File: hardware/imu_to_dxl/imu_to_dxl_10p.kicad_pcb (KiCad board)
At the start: 2 copper layers, 141.9 x 72.9 mm, 867 parts, among them CN1 B3B-EH-A (LF)(SN), CN2 B3B-PH-K-S(LF)(SN), J1 1.8mm螺丝孔, J2 1.8mm螺丝孔, J3 1.8mm螺丝孔, J4 1.8mm螺丝孔, Q1 MMBT3906, U1 ETA2845S2G_C22362741, U2 GD32F303CCT6, U3 LSM6DSV16XTR, U4 SN74LVC1G126DBVR, U5 SN74LVC1G125DBV, U6 ME6211C18M5G-N, X1 XL2EL89CSI-111YLC-12M

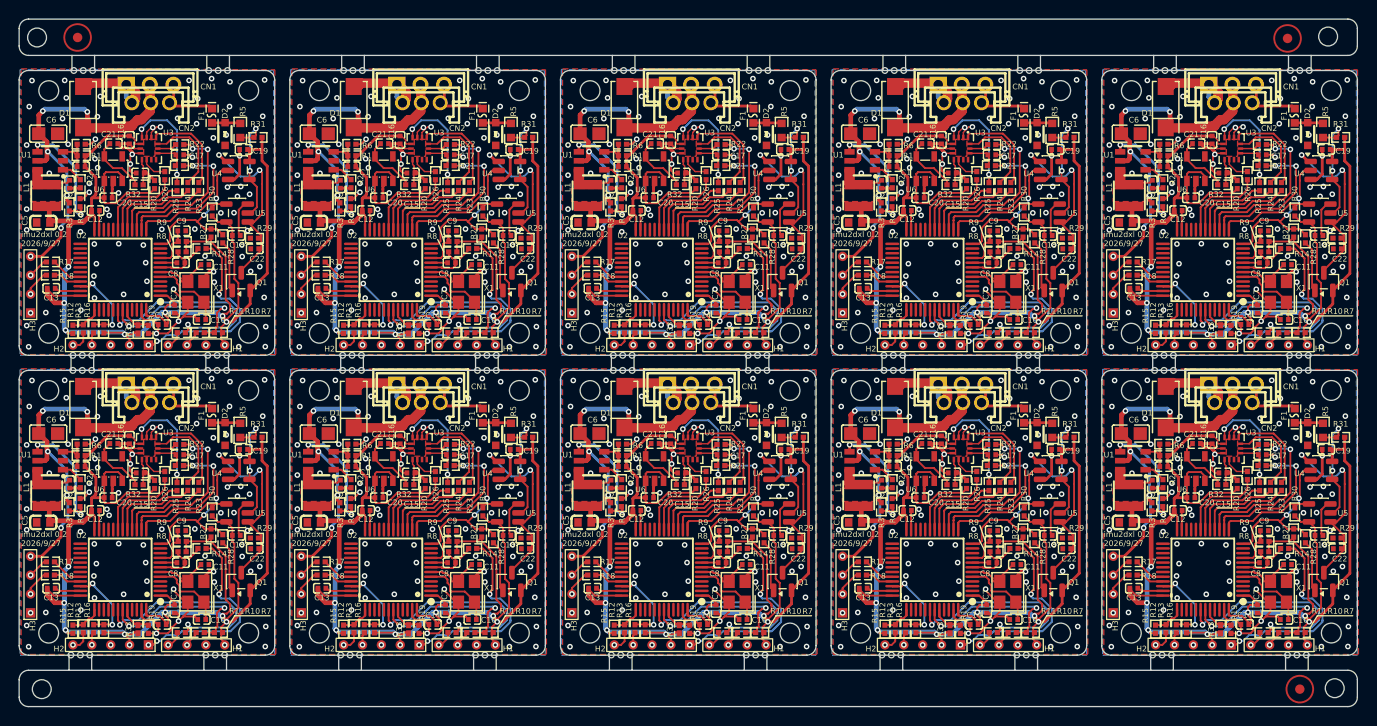
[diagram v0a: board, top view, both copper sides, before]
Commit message: 更新imu_to_dxl:1、优化MCU晶震电路；2、增加调试知识灯
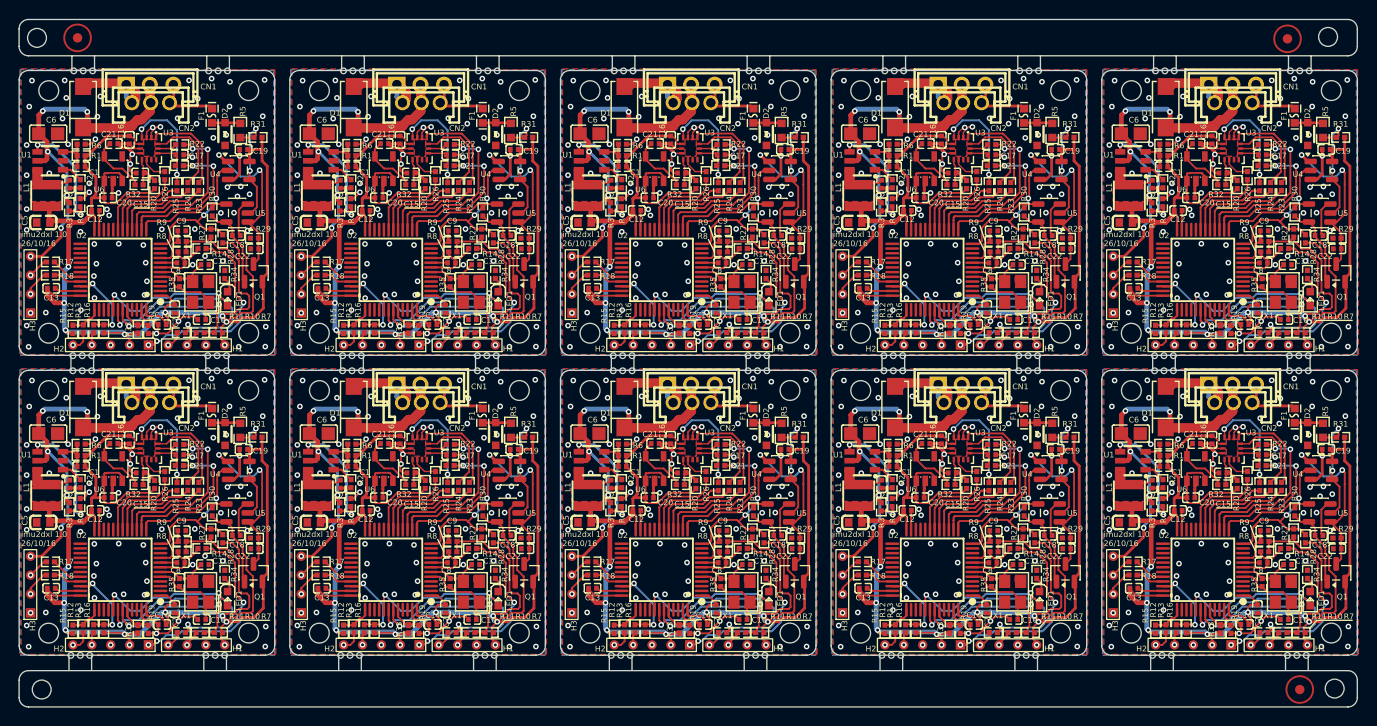
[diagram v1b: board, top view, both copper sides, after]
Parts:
- removed the Q1 at (133.6, 157.6)
- removed the Q1 at (162.2, 157.6)
- removed the Q1 at (76.2, 125.8)
- removed the Q1 at (190.9, 125.8)
- removed the Q1 at (76.2, 157.6)
- removed the Q1 at (162.2, 125.8)
- removed the Q1 at (104.8, 157.6)
- removed the Q1 at (133.6, 125.8)
- removed the Q1 at (104.8, 125.8)
- removed the REF** at (130.0, 103.4)
- removed the REF** at (189.3, 133.6)
- removed the REF** at (131.9, 135.2)
- removed the REF** at (72.6, 135.2)
- removed the REF** at (87.9, 135.2)
- removed the REF** at (60.1, 165.4)
- removed the REF** at (145.1, 165.4)
- removed the REF** at (55.0, 169.0)
- removed the REF** at (160.7, 103.4)
- removed the REF** at (187.4, 103.4)
- removed the REF** at (74.6, 133.6)
- removed the REF** at (116.7, 103.4)
- removed the REF** at (117.6, 135.2)
- removed the REF** at (116.4, 165.4)
- removed the REF** at (131.0, 103.4)
- removed the REF** at (72.7, 103.4)
- removed the REF** at (173.8, 165.4)
- removed the REF** at (145.3, 133.6)
- removed the REF** at (102.3, 103.4)
- removed the REF** at (160.6, 135.2)
- removed the REF** at (58.8, 99.9)
- removed the REF** at (87.7, 165.4)
- removed the REF** at (144.4, 103.4)
- removed the REF** at (103.2, 133.6)
- removed the REF** at (159.4, 165.4)
- removed the REF** at (131.9, 133.6)
- removed the REF** at (86.9, 133.6)
- removed the REF** at (60.3, 135.2)
- removed the REF** at (116.6, 135.2)
- removed the REF** at (160.4, 165.4)
- removed the REF** at (159.6, 133.6)
- removed the REF** at (131.7, 165.4)
- removed the REF** at (187.1, 100.0)
- removed the REF** at (88.0, 103.4)
- removed the REF** at (146.3, 135.2)
- removed the REF** at (173.1, 103.4)
- removed the REF** at (189.4, 103.4)
- removed the REF** at (188.4, 169.0)
- removed the REF** at (60.3, 133.6)
- removed the REF** at (58.3, 133.6)
- removed the REF** at (146.4, 103.4)
- removed the REF** at (102.2, 133.6)
- removed the REF** at (130.7, 165.4)
- removed the REF** at (129.9, 133.6)
- removed the REF** at (102.0, 165.4)
- removed the REF** at (174.8, 165.4)
- removed the REF** at (88.7, 165.4)
- removed the REF** at (117.7, 103.4)
- removed the REF** at (158.4, 165.4)
- removed the REF** at (115.6, 133.6)
- removed the REF** at (60.4, 103.4)
- removed the REF** at (101.3, 103.4)
- removed the REF** at (102.2, 135.2)
- removed the REF** at (144.3, 135.2)
- removed the REF** at (59.4, 103.4)
- removed the REF** at (132.0, 103.4)
- removed the REF** at (59.3, 133.6)
- removed the REF** at (159.6, 135.2)
- removed the REF** at (173.0, 133.6)
- removed the REF** at (130.9, 135.2)
- removed the REF** at (103.2, 135.2)
- removed the REF** at (158.6, 133.6)
- removed the REF** at (58.4, 103.4)
- removed the REF** at (189.1, 165.4)
- removed the REF** at (130.9, 133.6)
- removed the REF** at (188.3, 135.2)
- removed the REF** at (174.0, 135.2)
- removed the REF** at (103.3, 103.4)
- removed the REF** at (172.8, 165.4)
- removed the REF** at (144.1, 165.4)
- removed the REF** at (86.7, 165.4)
- removed the REF** at (87.9, 133.6)
- removed the REF** at (72.4, 165.4)
- removed the REF** at (175.1, 103.4)
- removed the REF** at (74.4, 165.4)
- removed the REF** at (187.3, 133.6)
- removed the REF** at (58.3, 135.2)
- removed the REF** at (188.1, 165.4)
- removed the REF** at (59.1, 165.4)
- removed the REF** at (188.4, 103.4)
- removed the REF** at (115.6, 135.2)
- removed the REF** at (73.7, 103.4)
- removed the REF** at (145.3, 135.2)
- removed the REF** at (146.1, 165.4)
- removed the REF** at (58.1, 165.4)
- removed the REF** at (116.6, 133.6)
- removed the REF** at (129.7, 165.4)
- removed the REF** at (187.1, 165.4)
- removed the REF** at (89.0, 103.4)
- removed the REF** at (101.2, 133.6)
- removed the REF** at (175.0, 135.2)
- removed the REF** at (145.4, 103.4)
- removed the REF** at (101.2, 135.2)
- removed the REF** at (173.0, 135.2)
- removed the REF** at (101.0, 165.4)
- removed the REF** at (72.6, 133.6)
- removed the REF** at (88.9, 133.6)
- removed the REF** at (160.6, 133.6)
- removed the REF** at (129.9, 135.2)
- removed the REF** at (187.3, 135.2)
- removed the REF** at (188.3, 133.6)
- removed the REF** at (144.3, 133.6)
- removed the REF** at (74.7, 103.4)
- removed the REF** at (158.7, 103.4)
- removed the REF** at (73.6, 133.6)
- removed the REF** at (115.4, 165.4)
- removed the REF** at (174.0, 133.6)
- removed the REF** at (189.3, 135.2)
- removed the REF** at (87.0, 103.4)
- removed the REF** at (146.3, 133.6)
- removed the REF** at (191.4, 99.8)
- removed the REF** at (174.1, 103.4)
- removed the REF** at (54.5, 99.9)
- removed the REF** at (175.0, 133.6)
- removed the REF** at (159.7, 103.4)
- removed the REF** at (192.1, 168.9)
- removed the REF** at (88.9, 135.2)
- removed the REF** at (74.6, 135.2)
- removed the REF** at (59.3, 135.2)
- removed the REF** at (73.6, 135.2)
- removed the REF** at (117.6, 133.6)
- removed the REF** at (158.6, 135.2)
- removed the REF** at (117.4, 165.4)
- removed the REF** at (115.7, 103.4)
- removed the REF** at (73.4, 165.4)
- removed the REF** at (86.9, 135.2)
- removed the REF** at (103.0, 165.4)
- removed the X1 at (157.4, 126.9)
- removed the X1 at (71.3, 126.9)
- removed the X1 at (100.0, 158.7)
- removed the X1 at (128.7, 158.7)
- removed the X1 at (186.1, 126.9)
- removed the X1 at (100.0, 126.9)
- removed the X1 at (128.7, 126.9)
- removed the X1 at (71.3, 158.7)
- removed the X1 at (157.4, 158.7)
- added LED1: GL0603UG01, microduck:LED0603-RD, F.Cu at (160.8, 159.4)
- added LED1: GL0603UG01, microduck:LED0603-RD, F.Cu at (160.8, 127.6)
- added LED1: GL0603UG01, microduck:LED0603-RD, F.Cu at (189.5, 159.4)
- added LED1: GL0603UG01, microduck:LED0603-RD, F.Cu at (103.4, 127.6)
- added LED1: GL0603UG01, microduck:LED0603-RD, F.Cu at (74.7, 127.6)
- added LED1: GL0603UG01, microduck:LED0603-RD, F.Cu at (74.7, 159.4)
- added LED1: GL0603UG01, microduck:LED0603-RD, F.Cu at (189.5, 127.6)
- added LED1: GL0603UG01, microduck:LED0603-RD, F.Cu at (103.4, 159.4)
- added LED1: GL0603UG01, microduck:LED0603-RD, F.Cu at (132.1, 127.6)
- added LED1: GL0603UG01, microduck:LED0603-RD, F.Cu at (132.1, 159.4)
- added Q1: MMBT3906, Package_TO_SOT_SMD:SOT-23, F.Cu at (77.5, 124.9)
- added Q1: MMBT3906, Package_TO_SOT_SMD:SOT-23, F.Cu at (77.5, 156.7)
- added Q1: MMBT3906, Package_TO_SOT_SMD:SOT-23, F.Cu at (106.2, 156.7)
- added Q1: MMBT3906, Package_TO_SOT_SMD:SOT-23, F.Cu at (106.2, 124.9)
- added Q1: MMBT3906, Package_TO_SOT_SMD:SOT-23, F.Cu at (134.8, 156.7)
- added Q1: MMBT3906, Package_TO_SOT_SMD:SOT-23, F.Cu at (192.2, 124.9)
- added Q1: MMBT3906, Package_TO_SOT_SMD:SOT-23, F.Cu at (134.8, 124.9)
- added Q1: MMBT3906, Package_TO_SOT_SMD:SOT-23, F.Cu at (163.6, 156.7)
- added Q1: MMBT3906, Package_TO_SOT_SMD:SOT-23, F.Cu at (163.6, 124.9)
- added R34: 100K, microduck:R0402, F.Cu at (131.8, 125.0)
- added R34: 100K, microduck:R0402, F.Cu at (74.4, 156.8)
- added R34: 100K, microduck:R0402, F.Cu at (160.5, 156.8)
- added R34: 100K, microduck:R0402, F.Cu at (189.2, 125.0)
- added R34: 100K, microduck:R0402, F.Cu at (160.5, 125.0)
- added R34: 100K, microduck:R0402, F.Cu at (103.1, 156.8)
- added R34: 100K, microduck:R0402, F.Cu at (189.2, 156.8)
- added R34: 100K, microduck:R0402, F.Cu at (103.1, 125.0)
- added R34: 100K, microduck:R0402, F.Cu at (131.8, 156.8)
- added R34: 100K, microduck:R0402, F.Cu at (74.4, 125.0)
- added R35: 1M, microduck:R0402, F.Cu at (155.7, 157.7)
- added R35: 1M, microduck:R0402, F.Cu at (155.7, 125.9)
- added R35: 1M, microduck:R0402, F.Cu at (127.0, 157.7)
- added R35: 1M, microduck:R0402, F.Cu at (69.6, 125.9)
- added R35: 1M, microduck:R0402, F.Cu at (98.3, 125.9)
- added R35: 1M, microduck:R0402, F.Cu at (69.6, 157.7)
- added R35: 1M, microduck:R0402, F.Cu at (127.0, 125.9)
- added R35: 1M, microduck:R0402, F.Cu at (98.3, 157.7)
- added R35: 1M, microduck:R0402, F.Cu at (184.4, 157.7)
- added R35: 1M, microduck:R0402, F.Cu at (184.4, 125.9)
- added REF**: mailslot, microduck:mailslot, F.Cu at (58.3, 133.6)
- added REF**: mailslot, microduck:mailslot, F.Cu at (160.4, 165.4)
- added REF**: mailslot, microduck:mailslot, F.Cu at (188.4, 103.4)
- added REF**: mailslot, microduck:mailslot, F.Cu at (103.0, 165.4)
- added REF**: mailslot, microduck:mailslot, F.Cu at (160.6, 133.6)
- added REF**: mailslot, microduck:mailslot, F.Cu at (115.6, 135.2)
- added REF**: mailslot, microduck:mailslot, F.Cu at (160.6, 135.2)
- added REF**: mailslot, microduck:mailslot, F.Cu at (174.1, 103.4)
- added REF**: mailslot, microduck:mailslot, F.Cu at (103.2, 135.2)
- added REF**: Mark, microduck:Mark, F.Cu at (187.1, 100.0)
- added REF**: mailslot, microduck:mailslot, F.Cu at (73.4, 165.4)
- added REF**: mailslot, microduck:mailslot, F.Cu at (103.3, 103.4)
- added REF**: mailslot, microduck:mailslot, F.Cu at (74.6, 133.6)
- added REF**: mailslot, microduck:mailslot, F.Cu at (174.0, 135.2)
- added REF**: mailslot, microduck:mailslot, F.Cu at (117.6, 133.6)
- added REF**: mailslot, microduck:mailslot, F.Cu at (145.3, 133.6)
- added REF**: mailslot, microduck:mailslot, F.Cu at (189.1, 165.4)
- added REF**: mailslot, microduck:mailslot, F.Cu at (144.4, 103.4)
- added REF**: mailslot, microduck:mailslot, F.Cu at (72.6, 135.2)
- added REF**: mailslot, microduck:mailslot, F.Cu at (89.0, 103.4)
- added REF**: Mark, microduck:Mark, F.Cu at (188.4, 169.0)
- added REF**: mailslot, microduck:mailslot, F.Cu at (101.3, 103.4)
- added REF**: mailslot, microduck:mailslot, F.Cu at (131.9, 135.2)
- added REF**: mailslot, microduck:mailslot, F.Cu at (88.7, 165.4)
- added REF**: mailslot, microduck:mailslot, F.Cu at (131.7, 165.4)
- added REF**: mailslot, microduck:mailslot, F.Cu at (173.8, 165.4)
- added REF**: INS_HOLE, microduck:INS_HOLE, F.Cu at (191.4, 99.8)
- added REF**: mailslot, microduck:mailslot, F.Cu at (187.3, 133.6)
- added REF**: mailslot, microduck:mailslot, F.Cu at (159.7, 103.4)
- added REF**: mailslot, microduck:mailslot, F.Cu at (189.4, 103.4)
- added REF**: mailslot, microduck:mailslot, F.Cu at (116.6, 133.6)
- added REF**: INS_HOLE, microduck:INS_HOLE, F.Cu at (55.0, 169.0)
- added REF**: mailslot, microduck:mailslot, F.Cu at (60.3, 135.2)
- added REF**: mailslot, microduck:mailslot, F.Cu at (59.1, 165.4)
- added REF**: mailslot, microduck:mailslot, F.Cu at (115.6, 133.6)
- added REF**: mailslot, microduck:mailslot, F.Cu at (102.0, 165.4)
- added REF**: mailslot, microduck:mailslot, F.Cu at (144.3, 135.2)
- added REF**: INS_HOLE, microduck:INS_HOLE, F.Cu at (192.1, 168.9)
- added REF**: mailslot, microduck:mailslot, F.Cu at (101.0, 165.4)
- added REF**: mailslot, microduck:mailslot, F.Cu at (145.1, 165.4)
- added REF**: mailslot, microduck:mailslot, F.Cu at (103.2, 133.6)
- added REF**: mailslot, microduck:mailslot, F.Cu at (144.3, 133.6)
- added REF**: mailslot, microduck:mailslot, F.Cu at (88.0, 103.4)
- added REF**: mailslot, microduck:mailslot, F.Cu at (72.6, 133.6)
- added REF**: mailslot, microduck:mailslot, F.Cu at (188.3, 133.6)
- added REF**: mailslot, microduck:mailslot, F.Cu at (187.4, 103.4)
- added REF**: mailslot, microduck:mailslot, F.Cu at (159.4, 165.4)
- added REF**: mailslot, microduck:mailslot, F.Cu at (101.2, 135.2)
- added REF**: mailslot, microduck:mailslot, F.Cu at (132.0, 103.4)
- added REF**: mailslot, microduck:mailslot, F.Cu at (117.4, 165.4)
- added REF**: mailslot, microduck:mailslot, F.Cu at (60.1, 165.4)
- added REF**: mailslot, microduck:mailslot, F.Cu at (58.4, 103.4)
- added REF**: mailslot, microduck:mailslot, F.Cu at (72.7, 103.4)
- added REF**: INS_HOLE, microduck:INS_HOLE, F.Cu at (54.5, 99.9)
- added REF**: mailslot, microduck:mailslot, F.Cu at (175.0, 133.6)
- added REF**: mailslot, microduck:mailslot, F.Cu at (86.9, 135.2)
- added REF**: mailslot, microduck:mailslot, F.Cu at (160.7, 103.4)
- added REF**: mailslot, microduck:mailslot, F.Cu at (159.6, 135.2)
- added REF**: mailslot, microduck:mailslot, F.Cu at (115.7, 103.4)
- added REF**: mailslot, microduck:mailslot, F.Cu at (60.4, 103.4)
- added REF**: mailslot, microduck:mailslot, F.Cu at (174.0, 133.6)
- added REF**: mailslot, microduck:mailslot, F.Cu at (74.7, 103.4)
- added REF**: mailslot, microduck:mailslot, F.Cu at (117.6, 135.2)
- added REF**: mailslot, microduck:mailslot, F.Cu at (146.4, 103.4)
- added REF**: mailslot, microduck:mailslot, F.Cu at (59.3, 135.2)
- added REF**: mailslot, microduck:mailslot, F.Cu at (59.4, 103.4)
- added REF**: mailslot, microduck:mailslot, F.Cu at (116.7, 103.4)
- added REF**: mailslot, microduck:mailslot, F.Cu at (87.9, 135.2)
- added REF**: mailslot, microduck:mailslot, F.Cu at (130.7, 165.4)
- added REF**: mailslot, microduck:mailslot, F.Cu at (73.6, 135.2)
- added REF**: mailslot, microduck:mailslot, F.Cu at (145.4, 103.4)
- added REF**: mailslot, microduck:mailslot, F.Cu at (74.6, 135.2)
- added REF**: mailslot, microduck:mailslot, F.Cu at (188.1, 165.4)
- added REF**: mailslot, microduck:mailslot, F.Cu at (87.7, 165.4)
- added REF**: mailslot, microduck:mailslot, F.Cu at (87.0, 103.4)
- added REF**: mailslot, microduck:mailslot, F.Cu at (60.3, 133.6)
- added REF**: mailslot, microduck:mailslot, F.Cu at (102.2, 133.6)
- added REF**: mailslot, microduck:mailslot, F.Cu at (172.8, 165.4)
- added REF**: mailslot, microduck:mailslot, F.Cu at (158.6, 135.2)
- added REF**: Mark, microduck:Mark, F.Cu at (58.8, 99.9)
- added REF**: mailslot, microduck:mailslot, F.Cu at (146.1, 165.4)
- added REF**: mailslot, microduck:mailslot, F.Cu at (131.0, 103.4)
- added REF**: mailslot, microduck:mailslot, F.Cu at (72.4, 165.4)
- added REF**: mailslot, microduck:mailslot, F.Cu at (175.1, 103.4)
- added REF**: mailslot, microduck:mailslot, F.Cu at (158.6, 133.6)
- added REF**: mailslot, microduck:mailslot, F.Cu at (129.7, 165.4)
- added REF**: mailslot, microduck:mailslot, F.Cu at (58.1, 165.4)
- added REF**: mailslot, microduck:mailslot, F.Cu at (129.9, 133.6)
- added REF**: mailslot, microduck:mailslot, F.Cu at (115.4, 165.4)
- added REF**: mailslot, microduck:mailslot, F.Cu at (102.2, 135.2)
- added REF**: mailslot, microduck:mailslot, F.Cu at (188.3, 135.2)
- added REF**: mailslot, microduck:mailslot, F.Cu at (130.0, 103.4)
- added REF**: mailslot, microduck:mailslot, F.Cu at (130.9, 135.2)
- added REF**: mailslot, microduck:mailslot, F.Cu at (116.4, 165.4)
- added REF**: mailslot, microduck:mailslot, F.Cu at (189.3, 133.6)
- added REF**: mailslot, microduck:mailslot, F.Cu at (158.4, 165.4)
- added REF**: mailslot, microduck:mailslot, F.Cu at (116.6, 135.2)
- added REF**: mailslot, microduck:mailslot, F.Cu at (173.0, 135.2)
- added REF**: mailslot, microduck:mailslot, F.Cu at (88.9, 133.6)
- added REF**: mailslot, microduck:mailslot, F.Cu at (101.2, 133.6)
- added REF**: mailslot, microduck:mailslot, F.Cu at (86.7, 165.4)
- added REF**: mailslot, microduck:mailslot, F.Cu at (73.6, 133.6)
- added REF**: mailslot, microduck:mailslot, F.Cu at (102.3, 103.4)
- added REF**: mailslot, microduck:mailslot, F.Cu at (146.3, 133.6)
- added REF**: mailslot, microduck:mailslot, F.Cu at (187.3, 135.2)
- added REF**: mailslot, microduck:mailslot, F.Cu at (189.3, 135.2)
- added REF**: mailslot, microduck:mailslot, F.Cu at (131.9, 133.6)
- added REF**: mailslot, microduck:mailslot, F.Cu at (145.3, 135.2)
- added REF**: mailslot, microduck:mailslot, F.Cu at (129.9, 135.2)
- added REF**: mailslot, microduck:mailslot, F.Cu at (146.3, 135.2)
- added REF**: mailslot, microduck:mailslot, F.Cu at (159.6, 133.6)
- added REF**: mailslot, microduck:mailslot, F.Cu at (59.3, 133.6)
- added REF**: mailslot, microduck:mailslot, F.Cu at (175.0, 135.2)
- added REF**: mailslot, microduck:mailslot, F.Cu at (144.1, 165.4)
- added REF**: mailslot, microduck:mailslot, F.Cu at (117.7, 103.4)
- added REF**: mailslot, microduck:mailslot, F.Cu at (187.1, 165.4)
- added REF**: mailslot, microduck:mailslot, F.Cu at (173.1, 103.4)
- added REF**: mailslot, microduck:mailslot, F.Cu at (174.8, 165.4)
- added REF**: mailslot, microduck:mailslot, F.Cu at (173.0, 133.6)
- added REF**: mailslot, microduck:mailslot, F.Cu at (87.9, 133.6)
- added REF**: mailslot, microduck:mailslot, F.Cu at (74.4, 165.4)
- added REF**: mailslot, microduck:mailslot, F.Cu at (86.9, 133.6)
- added REF**: mailslot, microduck:mailslot, F.Cu at (88.9, 135.2)
- added REF**: mailslot, microduck:mailslot, F.Cu at (158.7, 103.4)
- added REF**: mailslot, microduck:mailslot, F.Cu at (58.3, 135.2)
- added REF**: mailslot, microduck:mailslot, F.Cu at (130.9, 133.6)
- added REF**: mailslot, microduck:mailslot, F.Cu at (73.7, 103.4)
- added X1: XL2EL89CSI-111YLC-12M, microduck:CRYSTAL-SMD_4P-L3.2-W2.5-BL, F.Cu at (129.2, 126.9)
- added X1: XL2EL89CSI-111YLC-12M, microduck:CRYSTAL-SMD_4P-L3.2-W2.5-BL, F.Cu at (186.7, 126.9)
- added X1: XL2EL89CSI-111YLC-12M, microduck:CRYSTAL-SMD_4P-L3.2-W2.5-BL, F.Cu at (100.5, 158.7)
- added X1: XL2EL89CSI-111YLC-12M, microduck:CRYSTAL-SMD_4P-L3.2-W2.5-BL, F.Cu at (157.9, 126.9)
- added X1: XL2EL89CSI-111YLC-12M, microduck:CRYSTAL-SMD_4P-L3.2-W2.5-BL, F.Cu at (157.9, 158.7)
- added X1: XL2EL89CSI-111YLC-12M, microduck:CRYSTAL-SMD_4P-L3.2-W2.5-BL, F.Cu at (129.2, 158.7)
- added X1: XL2EL89CSI-111YLC-12M, microduck:CRYSTAL-SMD_4P-L3.2-W2.5-BL, F.Cu at (100.5, 126.9)
- added X1: XL2EL89CSI-111YLC-12M, microduck:CRYSTAL-SMD_4P-L3.2-W2.5-BL, F.Cu at (71.8, 158.7)
- added X1: XL2EL89CSI-111YLC-12M, microduck:CRYSTAL-SMD_4P-L3.2-W2.5-BL, F.Cu at (71.8, 126.9)
- C10 (x10), C11 (x10): value 27pF/50V -> 20pF/50V
- CN1 (x10): value B3B-EH-A (LF)(SN) -> B3B-EH-A(LF)(SN)
- CN2 (x10): value B3B-PH-K-S(LF)(SN) -> AMP175778/8283/A2007WV-3P
- D1 (x10): value SMAJ24A -> SMAJ36A
- D2 (x10): value 3.3V ESD -> 5V ESD
- R31 (x10): value 10k -> 100k
- R5 (x10): value 100R -> 0R
- moved Q1 1.60 mm to (192.2, 156.7)
- moved X1 0.51 mm to (186.7, 158.7)
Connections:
- U2 pad 41: unconnected-(U2-PB5-Pad41) -> /DEBUG_LED (x10)
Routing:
- net /DEBUG_LED: track 0.00 -> 160.3 mm, vias 0 -> 20
- net +3.3V: track 1444.6 -> 1513.1 mm
- net GND: track 580.3 -> 526.9 mm, vias 780 -> 710
- net /TXD_EN: track 202.6 -> 185.5 mm
- net Net-(LED1-K): track 0.00 -> 15.9 mm
- net /DEBUG_RX: track 176.0 -> 171.9 mm
- net /GD_OSCIN: track 83.1 -> 86.0 mm
- net Net-(Q1-B): track 54.6 -> 56.6 mm
- net /DEBUG_TX: track 229.4 -> 228.4 mm
- net /GD_OSCOUT: track 58.9 -> 59.8 mm
- net Net-(H2-Pad1): track 211.4 -> 212.1 mm
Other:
- outline, holes or cut-outs redrawn
- board text added: "imu2dxl 1.0 26/10/16"
- board text removed: "imu2dxl 0.2 2026/9/27"
